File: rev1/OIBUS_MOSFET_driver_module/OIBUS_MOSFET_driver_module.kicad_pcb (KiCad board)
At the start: 2 copper layers, 90.2 x 95.9 mm, 154 parts, among them J1 SWD, J10 +, J11 +, J12 +, J13 +, J14 UAVCAN JST GH, J2 UART, J3 5V - 24V, Molex Ultrafit, J4 +, J5 +, J6 +, J7 +, J8 +, J9 +, T1 DMG6402LVT, T10 DMG6402LVT, T2 DMG6402LVT, T3 DMG6402LVT, T4 DMG6402LVT, T5 DMG6402LVT, T6 DMG6402LVT, T7 DMG6402LVT, T8 DMG6402LVT, T9 DMG6402LVT, U1 TLP291, U10 STM32F303CCTx, U11 TLP291, U12 TLP291, U2 TLP291, U3 TLP291, U4 TLP291, U5 TLP291, U6 TLP291, U7 TLP291, U8 TLP291, U9 TCAN330, Y1 16M

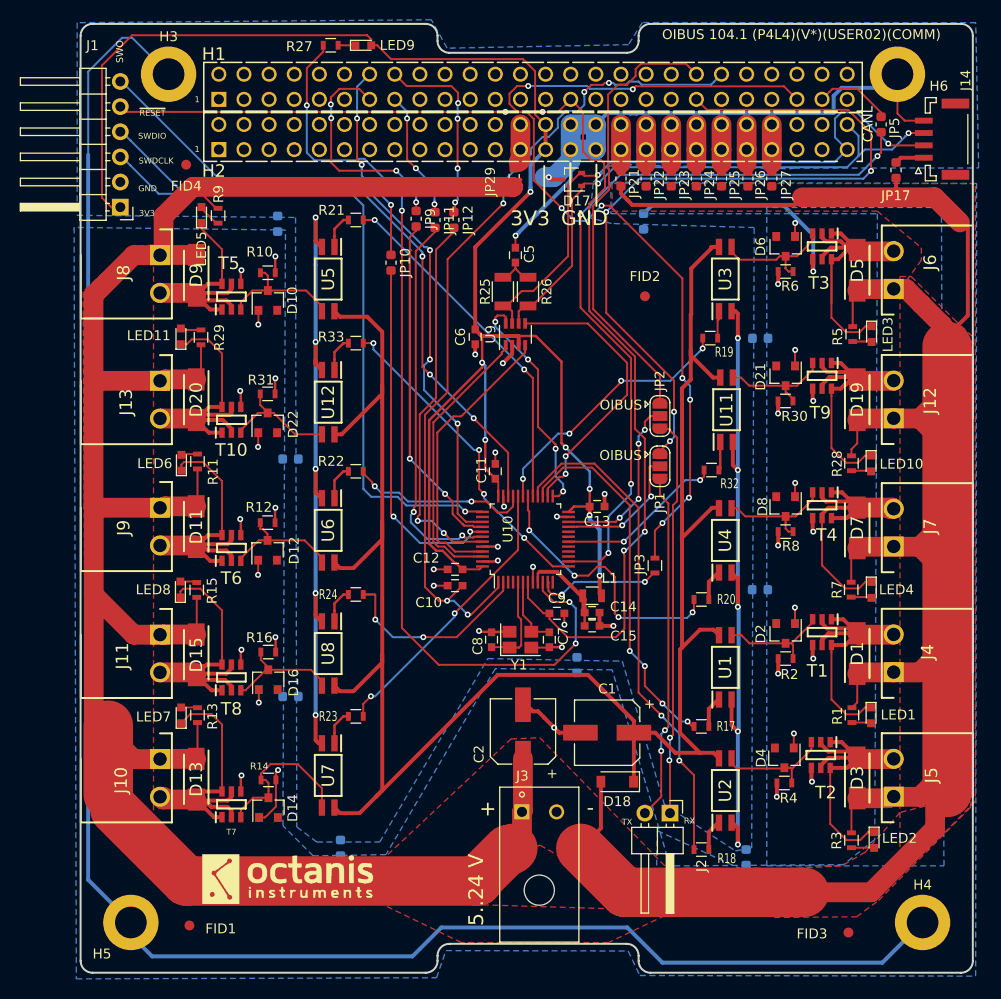
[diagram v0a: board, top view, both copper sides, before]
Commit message: redesigned for manufacturing, generated PCBA gerber and BOM files
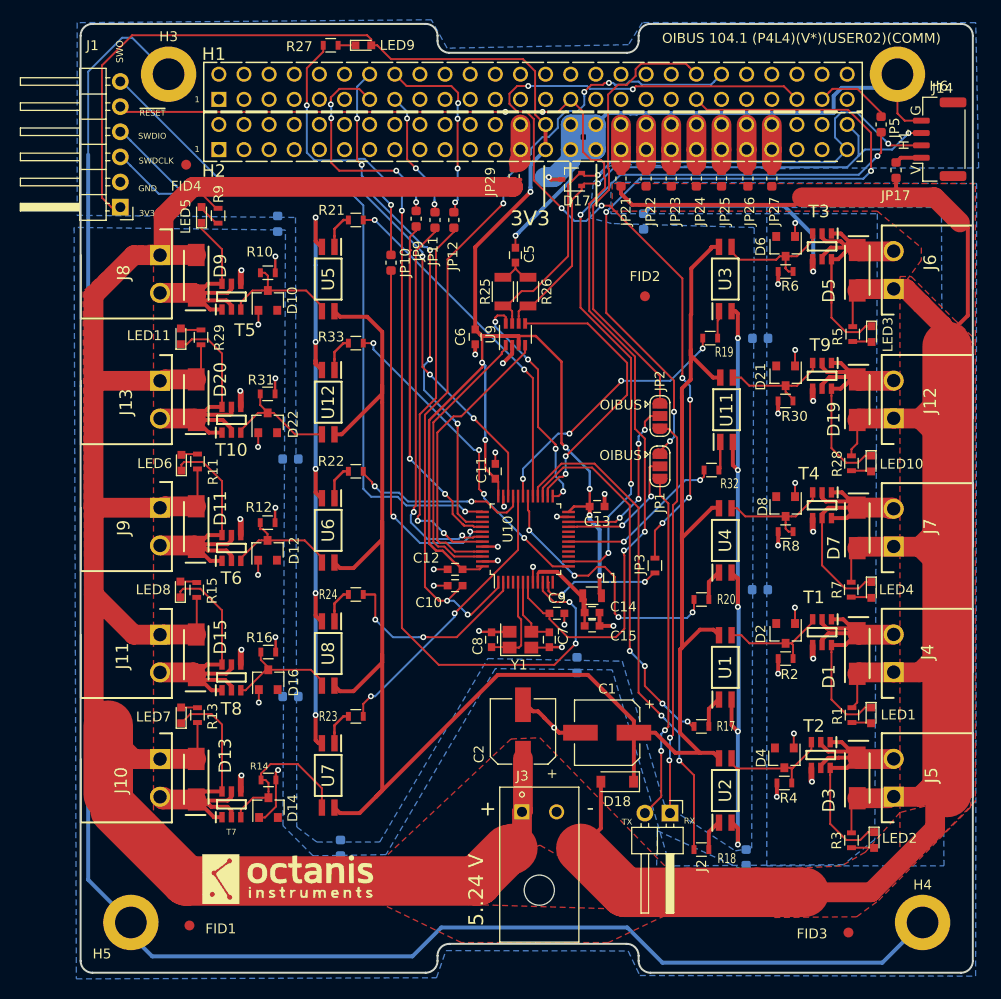
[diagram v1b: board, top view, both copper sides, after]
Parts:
- J14: footprint Connectors_JST:JST_GH_SM04B-GHS-TB_04x1.25mm_Angled -> lib_fp_global:uavcan_connector
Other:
- board text removed: "CANL"
